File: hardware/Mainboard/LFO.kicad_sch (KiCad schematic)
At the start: 19 parts, among them Q1 2N3904, Q16 2N3904, Q17 2N3904, U6 TL074

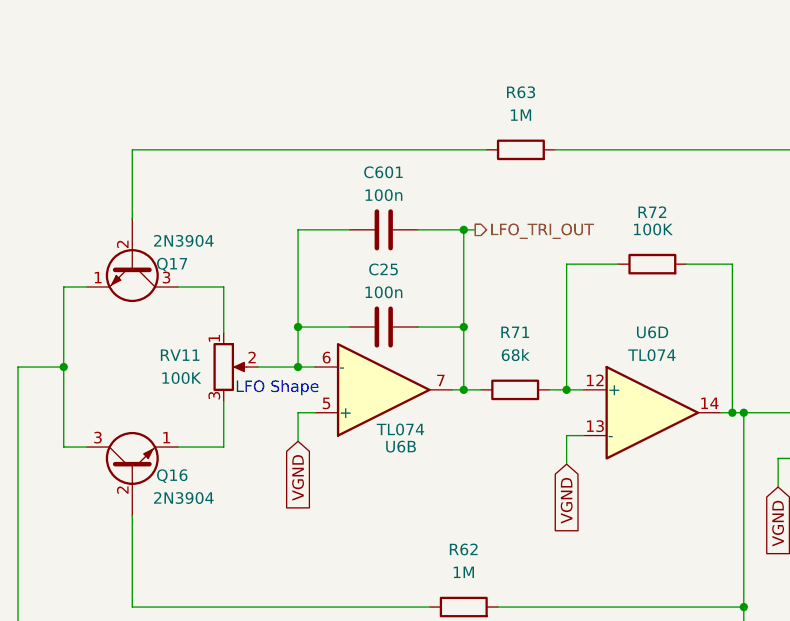
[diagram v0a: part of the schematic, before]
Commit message: add 0v2 status
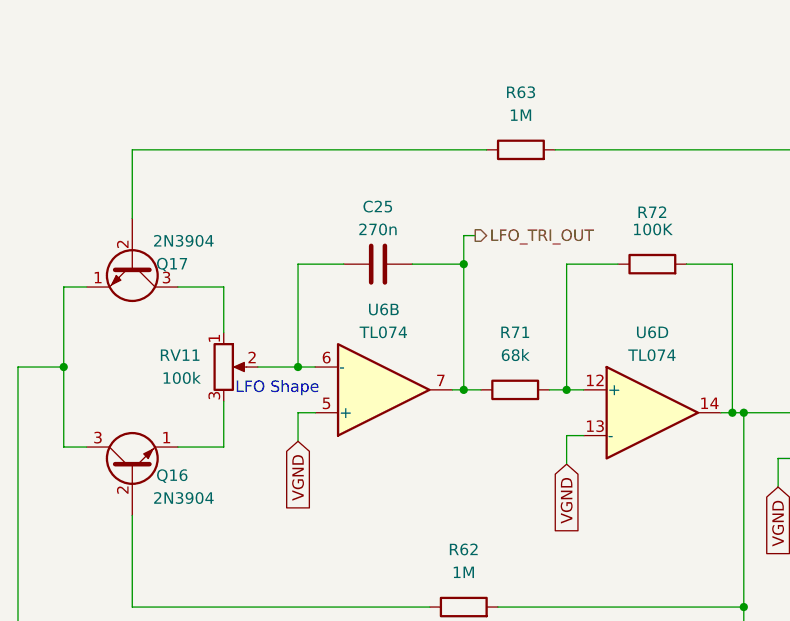
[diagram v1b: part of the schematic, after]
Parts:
- removed C601: 100n, Capacitor_THT:C_Rect_L7.2mm_W2.5mm_P5.00mm_FKS2_FKP2_MKS2_MKP2, symbol Device:C
- C25: value 100n -> 270n; footprint Capacitor_THT:C_Rect_L7.2mm_W2.5mm_P5.00mm_FKS2_FKP2_MKS2_MKP2 -> Capacitor_THT:C_Rect_L7.2mm_W5.5mm_P5.00mm_FKS2_FKP2_MKS2_MKP2
- RV11: value 100K -> 100k
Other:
- moved on the sheet: C25
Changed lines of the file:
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@@
   (junction (at 163.83 78.74) (diameter 0) (color 0 0 0 0)
   )
+  (junction (at 133.985 62.23) (diameter 0) (color 0 0 0 0)
+  )
   (junction (at 89.535 73.66) (diameter 0) (color 0 0 0 0)
   )
   (junction (at 165.1 100.33) (diameter 0) (color 0 0 0 0)
   )
-  (junction (at 115.57 69.215) (diameter 0) (color 0 0 0 0)
-  )
   (junction (at 165.1 78.74) (diameter 0) (color 0 0 0 0)
   )
@@
   (junction (at 115.57 73.66) (diameter 0) (color 0 0 0 0)
   )
-  (junction (at 133.985 69.215) (diameter 0) (color 0 0 0 0)
-  )
-  (junction (at 133.985 58.42) (diameter 0) (color 0 0 0 0)
-  )
   (wire (pts (xy 189.23 49.53) (xy 189.23 62.23))
     (stroke (width 0) (type default))
@@
     (stroke (width 0) (type default))
   )
-  (wire (pts (xy 128.905 69.215) (xy 133.985 69.215))
-    (stroke (width 0) (type default))
-  )
   (wire (pts (xy 137.795 117.475) (xy 161.29 117.475))
     (stroke (width 0) (type default))
   )
-  (wire (pts (xy 115.57 58.42) (xy 121.285 58.42))
-    (stroke (width 0) (type default))
-  )
   (wire (pts (xy 217.17 53.34) (xy 217.17 57.15))
     (stroke (width 0) (type default))
@@
     (stroke (width 0) (type default))
   )
+  (wire (pts (xy 133.985 62.23) (xy 133.985 76.2))
+    (stroke (width 0) (type default))
+  )
   (wire (pts (xy 144.145 49.53) (xy 189.23 49.53))
     (stroke (width 0) (type default))
   )
-  (wire (pts (xy 115.57 58.42) (xy 115.57 69.215))
+  (wire (pts (xy 115.57 62.23) (xy 115.57 73.66))
     (stroke (width 0) (type default))
   )
@@
     (stroke (width 0) (type default))
   )
-  (wire (pts (xy 133.985 58.42) (xy 135.255 58.42))
+  (wire (pts (xy 133.985 59.055) (xy 135.255 59.055))
+    (stroke (width 0) (type default))
+  )
+  (wire (pts (xy 128.27 62.23) (xy 133.985 62.23))
     (stroke (width 0) (type default))
   )
@@
     (stroke (width 0) (type default))
   )
+  (wire (pts (xy 120.65 62.23) (xy 115.57 62.23))
+    (stroke (width 0) (type default))
+  )
   (wire (pts (xy 163.83 62.23) (xy 163.83 78.74))
     (stroke (width 0) (type default))
@@
     (stroke (width 0) (type default))
   )
-  (wire (pts (xy 115.57 69.215) (xy 115.57 73.66))
-    (stroke (width 0) (type default))
-  )
   (wire (pts (xy 189.23 81.28) (xy 186.69 81.28))
     (stroke (width 0) (type default))
@@
     (stroke (width 0) (type default))
   )
-  (wire (pts (xy 133.985 69.215) (xy 133.985 76.2))
-    (stroke (width 0) (type default))
-  )
   (wire (pts (xy 111.125 73.66) (xy 115.57 73.66))
     (stroke (width 0) (type default))
   )
-  (wire (pts (xy 128.905 58.42) (xy 133.985 58.42))
-    (stroke (width 0) (type default))
-  )
   (wire (pts (xy 102.235 64.77) (xy 107.315 64.77))
     (stroke (width 0) (type default))
@@
     (stroke (width 0) (type default))
   )
-  (wire (pts (xy 133.985 58.42) (xy 133.985 69.215))
-    (stroke (width 0) (type default))
-  )
   (wire (pts (xy 217.17 77.47) (xy 217.17 80.01))
     (stroke (width 0) (type default))
@@
     (stroke (width 0) (type default))
   )
-  (wire (pts (xy 115.57 69.215) (xy 121.285 69.215))
+  (wire (pts (xy 133.985 59.055) (xy 133.985 62.23))
     (stroke (width 0) (type default))
   )
@@
     )
   )
-  (hierarchical_label "LFO_TRI_OUT" (shape output) (at 135.255 58.42 0) (fields_autoplaced)
+  (hierarchical_label "LFO_TRI_OUT" (shape output) (at 135.255 59.055 0) (fields_autoplaced)
     (effects (font (size 1.27 1.27)) (justify left))
   )
@@
     )
   )
-  (symbol (lib_id "Device:C") (at 125.095 58.42 90) (unit 1)
-    (in_bom yes) (on_board yes) (dnp no) (fields_autoplaced)
-    (property "Reference" "C601" (at 125.095 52.07 90)
-      (effects (font (size 1.27 1.27)))
-    )
-    (property "Value" "100n" (at 125.095 54.61 90)
-      (effects (font (size 1.27 1.27)))
-    )
-    (property "Footprint" "Capacitor_THT:C_Rect_L7.2mm_W2.5mm_P5.00mm_FKS2_FKP2_MKS2_MKP2" (at 128.905 57.4548 0)
-      (effects (font (size 1.27 1.27)) hide)
-    )
-    (property "Datasheet" "~" (at 125.095 58.42 0)
-      (effects (font (size 1.27 1.27)) hide)
-    )
-    (pin "1")
-    (pin "2")
-    (instances
-      (project "LivSynth_Hardware"
-        (path "/f595cb10-48de-4dd8-91c0-2935f104b3c6/a8e2a098-2010-4ec0-a897-f9a91ed4a45e"
-          (reference "C601") (unit 1)
-        )
-      )
-    )
-  )
   (symbol (lib_id "power:GND") (at 217.17 90.17 0) (unit 1)
     (in_bom yes) (on_board yes) (dnp no) (fields_autoplaced)
@@
     )
   )
-  (symbol (lib_id "Device:C") (at 125.095 69.215 90) (unit 1)
-    (in_bom yes) (on_board yes) (dnp no) (fields_autoplaced)
-    (property "Reference" "C25" (at 125.095 62.865 90)
-      (effects (font (size 1.27 1.27)))
-    )
-    (property "Value" "100n" (at 125.095 65.405 90)
-      (effects (font (size 1.27 1.27)))
-    )
-    (property "Footprint" "Capacitor_THT:C_Rect_L7.2mm_W2.5mm_P5.00mm_FKS2_FKP2_MKS2_MKP2" (at 128.905 68.2498 0)
-      (effects (font (size 1.27 1.27)) hide)
-    )
-    (property "Datasheet" "~" (at 125.095 69.215 0)
+  (symbol (lib_id "Device:C") (at 124.46 62.23 90) (unit 1)
+    (in_bom yes) (on_board yes) (dnp no) (fields_autoplaced)
+    (property "Reference" "C25" (at 124.46 55.88 90)
+      (effects (font (size 1.27 1.27)))
+    )
+    (property "Value" "270n" (at 124.46 58.42 90)
+      (effects (font (size 1.27 1.27)))
+    )
+    (property "Footprint" "Capacitor_THT:C_Rect_L7.2mm_W5.5mm_P5.00mm_FKS2_FKP2_MKS2_MKP2" (at 128.27 61.2648 0)
+      (effects (font (size 1.27 1.27)) hide)
+    )
+    (property "Datasheet" "~" (at 124.46 62.23 0)
       (effects (font (size 1.27 1.27)) hide)
     )
@@
       (effects (font (size 1.27 1.27)) (justify right))
     )
-    (property "Value" "100K" (at 104.775 74.9299 0)
+    (property "Value" "100k" (at 104.775 74.9299 0)
       (effects (font (size 1.27 1.27)) (justify right))
     )
@@
   (symbol (lib_id "Amplifier_Operational:TL074") (at 125.095 76.2 0) (mirror x) (unit 2)
     (in_bom yes) (on_board yes) (dnp no)
-    (property "Reference" "U6" (at 127 82.55 0)
-      (effects (font (size 1.27 1.27)))
-    )
-    (property "Value" "TL074" (at 127 80.645 0)
-      (effects (font (size 1.27 1.27)))
-    )
+    (property "Reference" "U6" (at 125.095 67.31 0)
+      (effects (font (size 1.27 1.27)))
+    )
+    (property "Value" "TL074" (at 125.095 69.85 0)
+      (effects (font (size 1.27 1.27)))
+    )

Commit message: Backport from 0v3
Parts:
- RV11: value 100k -> 100K
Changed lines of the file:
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@@
       (effects (font (size 1.27 1.27)) (justify right))
     )
-    (property "Value" "100k" (at 104.775 74.9299 0)
+    (property "Value" "100K" (at 104.775 74.9299 0)
       (effects (font (size 1.27 1.27)) (justify right))
     )
